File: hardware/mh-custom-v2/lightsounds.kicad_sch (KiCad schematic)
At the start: 18 parts, among them J1 Conn_01x03_Male, J2 Conn_01x03_Female

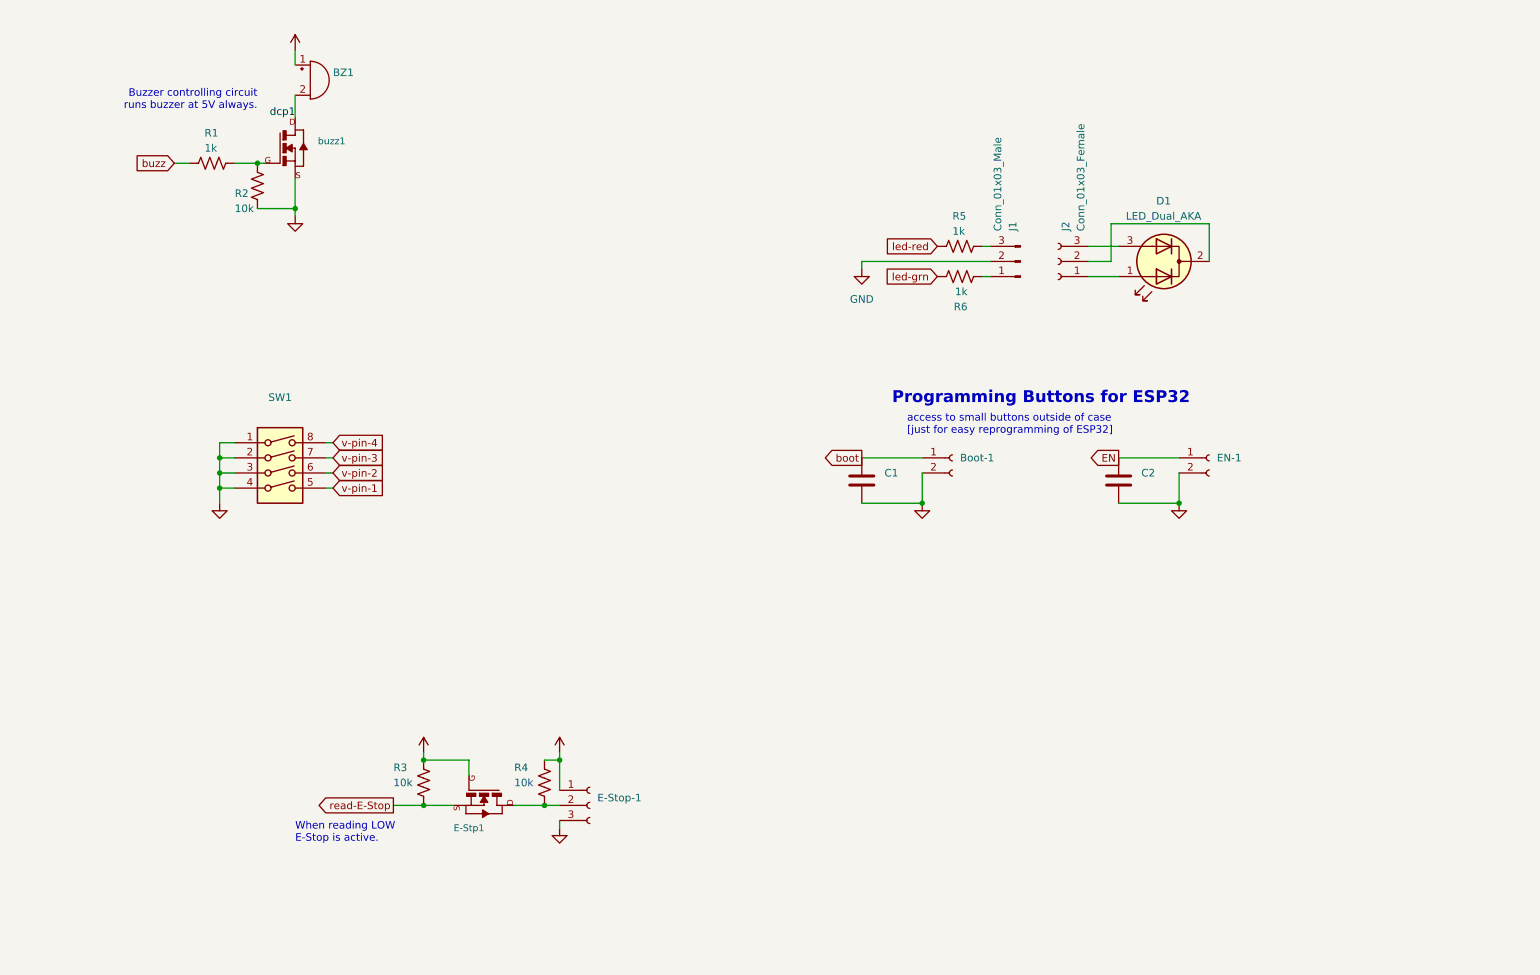
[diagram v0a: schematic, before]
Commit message: low-voltage side of V2 board rebuilt. Started on high-voltage side
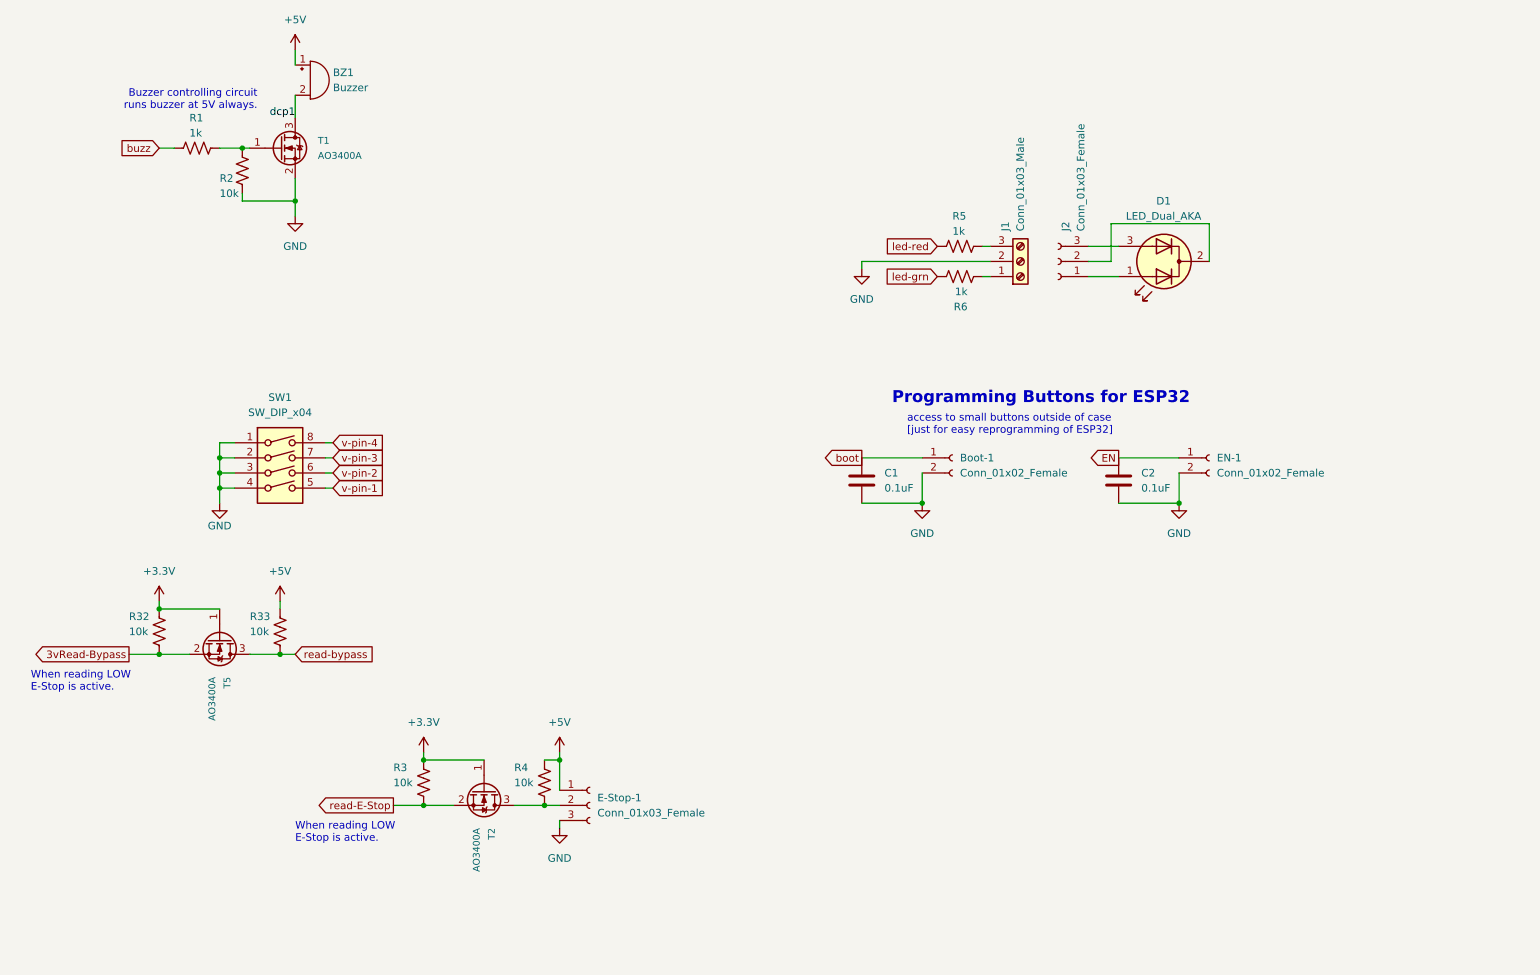
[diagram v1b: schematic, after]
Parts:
- removed E-Stp1: (no value), symbol Fab-Academy-2019:NMOSFETSOT23
- added R32, R33: 10k, Resistor_SMD:R_0603_1608Metric, symbol Device:R_US
- added T2, T5: AO3400A, Package_TO_SOT_SMD:SOT-23, symbol Transistor_FET:AO3400A
- BZ1: value (none) -> Buzzer; footprint (none) -> Buzzer_Beeper:Buzzer_15x7.5RM7.6
- Boot-1, EN-1: value (none) -> Conn_01x02_Female; footprint (none) -> Connector_PinSocket_2.54mm:PinSocket_1x02_P2.54mm_Vertical
- C1, C2: value (none) -> 0.1uF; footprint (none) -> LED_SMD:LED_0603_1608Metric
- D1: now left out of the parts list
- E-Stop-1: value (none) -> Conn_01x03_Female; footprint (none) -> Connector_JST:JST_PH_B3B-PH-K_1x03_P2.00mm_Vertical
- J1: footprint (none) -> TerminalBlock_TE-Connectivity:TerminalBlock_TE_282834-3_1x03_P2.54mm_Horizontal; symbol Connector:Conn_01x03_Male -> Connector:Screw_Terminal_01x03
- R1, R2, R4, R5, R6: footprint Resistor_SMD:R_1206_3216Metric_Pad1.30x1.75mm_HandSolder -> Resistor_SMD:R_0603_1608Metric
- R3: footprint (none) -> Resistor_SMD:R_0603_1608Metric
- SW1: value (none) -> SW_DIP_x04; footprint (none) -> Button_Switch_SMD:SW_DIP_SPSTx04_Slide_Omron_A6H-4101_W6.15mm_P1.27mm; JLCPCB Part # (none) -> C397291
- T1: renamed from buzz1; value (none) -> AO3400A; footprint (none) -> Package_TO_SOT_SMD:SOT-23; symbol Fab-Academy-2019:NMOSFETSOT23 -> Transistor_FET:AO3400A
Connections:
- net +3V3: now also R32.2, T2.1 (G), T5.1 (G)
- net +5V: now also R33.2
- net dcp1: now also T1.3 (D); no longer T1.1 (D)
- net read-E-Stop: now also T2.2 (S)
- net at R1.2, R2.2: now also T1.1 (G); no longer T1.3 (G)
- net at E-Stop-1.2 (Pin_2), R4.1: now also T2.3 (D)
- new net 3vRead-Bypass: R32.1, T5.2 (S)
- new net read-bypass: R33.1, T5.3 (D)
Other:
- moved on the sheet: R1, R2

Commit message: approaching ordering from JLCPCB
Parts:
- BZ1: JLCPCB Part # (none) -> C96095
- C1, C2: JLCPCB Part # (none) -> C14663
- J1: JLCPCB Part # (none) -> C557686
- R1, R5, R6: JLCPCB Part # (none) -> C21190
- R2, R3, R32, R33, R4: JLCPCB Part # (none) -> C25804
- T1, T2, T5: JLCPCB Part # (none) -> C427382
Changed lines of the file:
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@@
+      (effects (font (size 1.27 1.27)) hide)
+    )
+    (property "JLCPCB Part #" "C25804" (id 4) (at 48.26 130.81 0)
       (effects (font (size 1.27 1.27)) hide)
     )
@@
       (effects (font (size 1.27 1.27)) hide)
     )
+    (property "JLCPCB Part #" "C96095" (id 4) (at 73.66 38.1 0)
+      (effects (font (size 1.27 1.27)) hide)
+    )
     (pin "1")
     (pin "2")
@@
       (effects (font (size 1.27 1.27)) (justify left) hide)
     )
+    (property "JLCPCB Part #" "C427382" (id 4) (at 58.42 132.08 0)
+      (effects (font (size 1.27 1.27)) hide)
+    )
     (pin "1")
     (pin "2")
@@
       (effects (font (size 1.27 1.27)) hide)
     )
+    (property "JLCPCB Part #" "C25804" (id 4) (at 68.58 130.81 0)
+      (effects (font (size 1.27 1.27)) hide)
+    )
     (pin "1")
     (pin "2")
@@
     )
     (property "Datasheet" "~" (id 3) (at 182.88 66.04 0)
+      (effects (font (size 1.27 1.27)) hide)
+    )
+    (property "JLCPCB Part #" "C21190" (id 4) (at 182.88 66.04 90)
       (effects (font (size 1.27 1.27)) hide)
     )
@@
       (effects (font (size 1.27 1.27)) hide)
     )
+    (property "JLCPCB Part #" "C14663" (id 4) (at 166.37 105.41 0)
+      (effects (font (size 1.27 1.27)) hide)
+    )
     (pin "1")
     (pin "2")
@@
     )
     (property "Datasheet" "~" (id 3) (at 182.88 71.12 0)
+      (effects (font (size 1.27 1.27)) hide)
+    )
+    (property "JLCPCB Part #" "C21190" (id 4) (at 182.88 71.12 90)
       (effects (font (size 1.27 1.27)) hide)
     )
@@
       (effects (font (size 1.27 1.27)) (justify left) hide)
     )
+    (property "JLCPCB Part #" "C427382" (id 4) (at 102.87 157.48 0)
+      (effects (font (size 1.27 1.27)) hide)
+    )
     (pin "1")
     (pin "2")
@@
       (effects (font (size 1.27 1.27)) hide)
     )
+    (property "JLCPCB Part #" "C14663" (id 4) (at 209.55 105.41 0)
+      (effects (font (size 1.27 1.27)) hide)
+    )
     (pin "1")
     (pin "2")
@@
       (effects (font (size 1.27 1.27)) hide)
     )
+    (property "JLCPCB Part #" "C557686" (id 4) (at 193.04 68.58 90)
+      (effects (font (size 1.27 1.27)) hide)
+    )
     (pin "1")
     (pin "2")
@@
     )
     (property "Datasheet" "~" (id 3) (at 62.23 53.34 0)
+      (effects (font (size 1.27 1.27)) hide)
+    )
+    (property "JLCPCB Part #" "C25804" (id 4) (at 62.23 53.34 0)
       (effects (font (size 1.27 1.27)) hide)
     )
@@
       (effects (font (size 1.27 1.27)) hide)
     )
+    (property "JLCPCB Part #" "C25804" (id 4) (at 113.03 156.21 0)
+      (effects (font (size 1.27 1.27)) hide)
+    )
     (pin "1")
     (pin "2")
@@
     )
     (property "Datasheet" "~" (id 3) (at 54.61 49.53 0)
+      (effects (font (size 1.27 1.27)) hide)
+    )
+    (property "JLCPCB Part #" "C21190" (id 4) (at 54.61 49.53 90)
       (effects (font (size 1.27 1.27)) hide)
     )
@@
       (effects (font (size 1.27 1.27)) (justify left) hide)
     )
+    (property "JLCPCB Part #" "C427382" (id 4) (at 68.58 49.53 0)
+      (effects (font (size 1.27 1.27)) hide)
+    )
     (pin "1")
     (pin "2")
@@
       (effects (font (size 1.27 1.27)) hide)
     )
+    (property "JLCPCB Part #" "C25804" (id 4) (at 92.71 156.21 0)
+      (effects (font (size 1.27 1.27)) hide)
+    )

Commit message: prepping for JLCPCB order - all parts listed with numbers, BOM generated
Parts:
- E-Stop-1: JLCPCB Part # (none) -> C131339
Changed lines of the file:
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@@
+      (effects (font (size 1.27 1.27)) hide)
+    )
+    (property "JLCPCB Part #" "C131339" (id 4) (at 120.65 160.02 0)
       (effects (font (size 1.27 1.27)) hide)
     )

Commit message: finalizing details of ordering from JLCPCB
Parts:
- BZ1: footprint Buzzer_Beeper:Buzzer_15x7.5RM7.6 -> Buzzer_Beeper:Buzzer_12x9.5RM7.6
- SW1: JLCPCB Part # C397291 -> C224996
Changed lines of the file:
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@@
       (effects (font (size 1.27 1.27)) hide)
     )
-    (property "JLCPCB Part #" "C397291" (id 4) (at 68.58 104.14 0)
+    (property "JLCPCB Part #" "C224996" (id 4) (at 68.58 104.14 0)
       (effects (font (size 1.27 1.27)) hide)
     )
@@
       (effects (font (size 1.27 1.27)) (justify left))
     )
-    (property "Footprint" "Buzzer_Beeper:Buzzer_15x7.5RM7.6" (id 2) (at 73.025 35.56 90)
+    (property "Footprint" "Buzzer_Beeper:Buzzer_12x9.5RM7.6" (id 2) (at 73.025 35.56 90)
       (effects (font (size 1.27 1.27)) hide)
     )

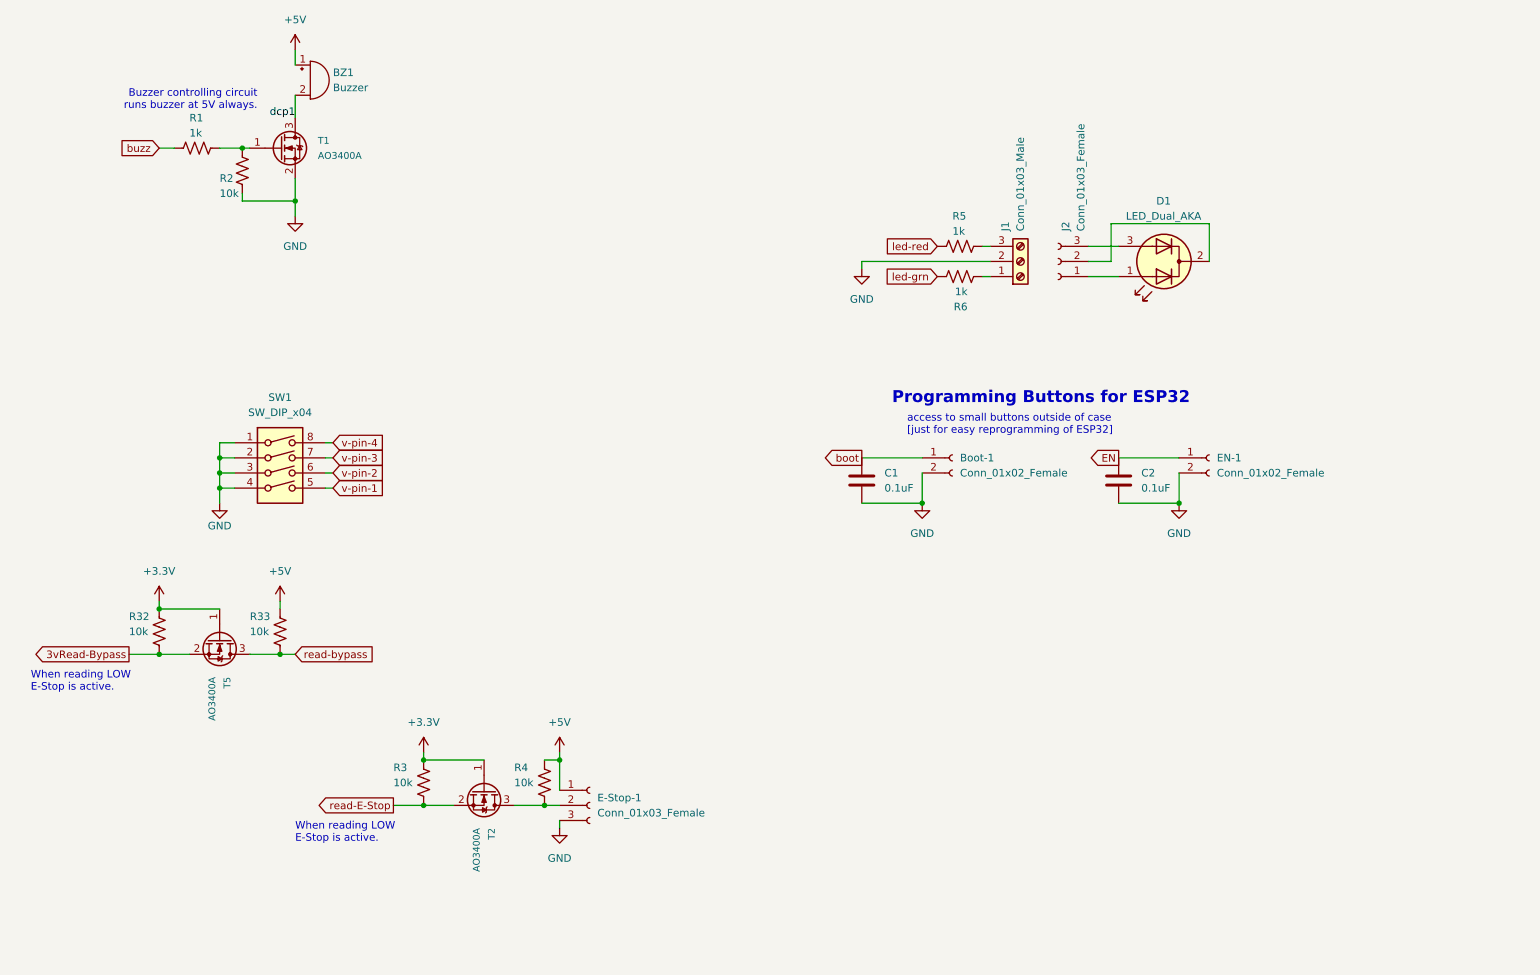
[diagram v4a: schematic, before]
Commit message: improved some of the connections for easier soldering/production
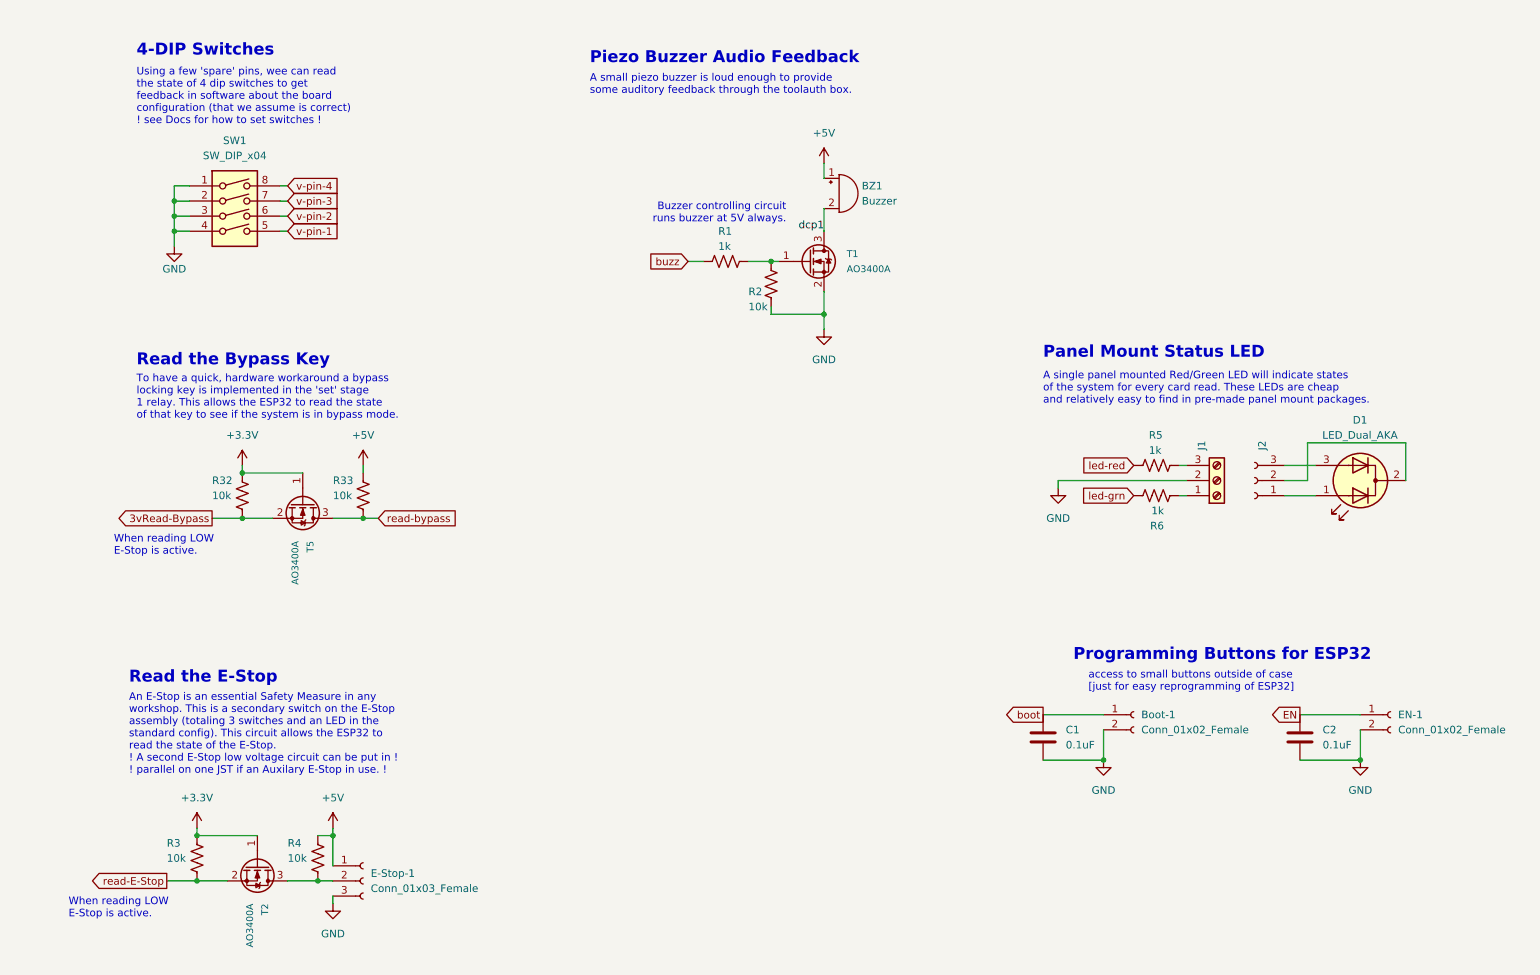
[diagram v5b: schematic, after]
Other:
- note added: "4-DIP Switches"
- note added: "A single panel mounted Red/Green LED will indicate states of the system for every card read. These LEDs are cheap and relatively easy to find in pre-made panel mount packages."
- note added: "A small piezo buzzer is loud enough to provide some auditory feedback through the toolauth box."
- note added: "An E-Stop is an essential Safety Measure in any workshop. This is a secondary switch on the E-Stop assembly (totaling 3 switches and an LED in the standard config). This circuit allows the ESP32 to read the state of the E-Stop. ! A second E-Stop low voltage circuit can be put in ! ! parallel on one JST if an Auxilary E-Stop in use. !"
- note added: "Panel Mount Status LED"
- note added: "Piezo Buzzer Audio Feedback"
- note added: "Read the Bypass Key"
- note added: "Read the E-Stop"
- note added: "To have a quick, hardware workaround a bypass locking key is implemented in the 'set' stage 1 relay. This allows the ESP32 to read the state of that key to see if the system is in bypass mode."
- note added: "Using a few 'spare' pins, wee can read the state of 4 dip switches to get feedback in software about the board configuration (that we assume is correct) ! see Docs for how to set switches !"
- moved on the sheet: BZ1, Boot-1, C1, C2, D1, E-Stop-1, EN-1, J1, J2, R1, R2, R3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
